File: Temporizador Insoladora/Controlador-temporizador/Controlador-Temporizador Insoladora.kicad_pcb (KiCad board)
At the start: 2 copper layers, 99.1 x 66 mm, 77 parts, among them P1 ICSP, P2 VAC12V, P3 CARGA, P4 TRANSF, P5 VAC, P6 OPTO, P7 CONN_02X08, P8 OPTO, P9 OPTO, Q1 BC548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

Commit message: Casi terminado controlador
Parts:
- moved C5 8.95 mm to (113.0, 116.2), turned to 180 degrees
- moved C13 3.81 mm to (193.7, 102.2)
- moved F1 3.81 mm to (174.6, 90.8)
- moved P3 3.81 mm to (210.2, 75.6)
- moved P4 3.81 mm to (200.0, 75.6)
- moved P5 3.81 mm to (187.3, 75.6)
- moved P8 3.81 mm to (184.8, 121.9)
- moved R15 3.81 mm to (188.6, 116.2)
- moved R18 3.81 mm to (182.2, 94.6)
- moved R19 3.81 mm to (187.3, 90.8)
- moved R23 3.81 mm to (191.1, 94.6)
- moved U3 3.81 mm to (184.8, 107.3)
- moved U4 3.81 mm to (194.9, 94.6)
- moved VR1 3.81 mm to (194.9, 81.9)
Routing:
- net VCC: track 134.1 -> 78.2 mm, vias 2 -> 3
- net Net-(D2-Pad1): track 22.6 -> 18.8 mm
- net Net-(D6-Pad1): track 6.66 -> 10.3 mm, vias 0 -> 1
- added copper zone on B.Cu, net VCC
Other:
- board size 99.1 x 66 mm -> 101.6 x 68.6 mm

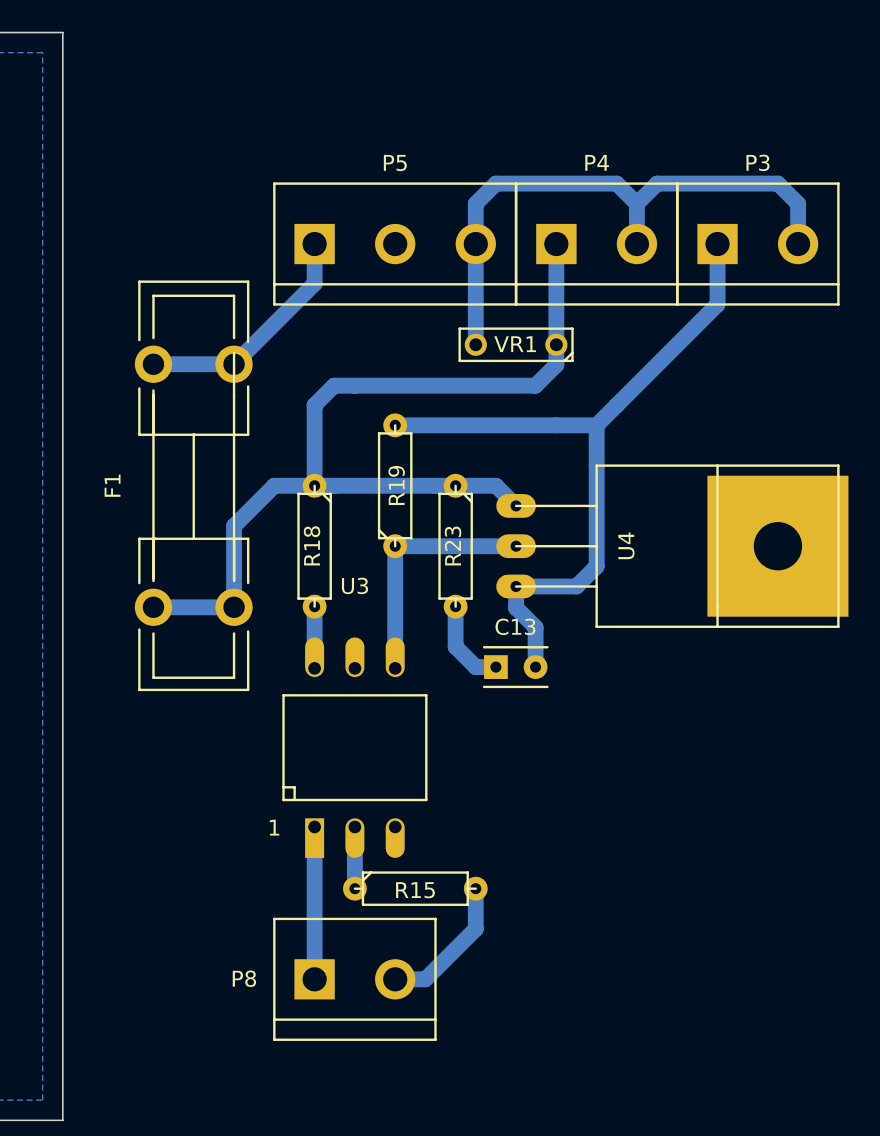
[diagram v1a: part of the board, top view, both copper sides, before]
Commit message: Acomodando la parte de potencia del controlador
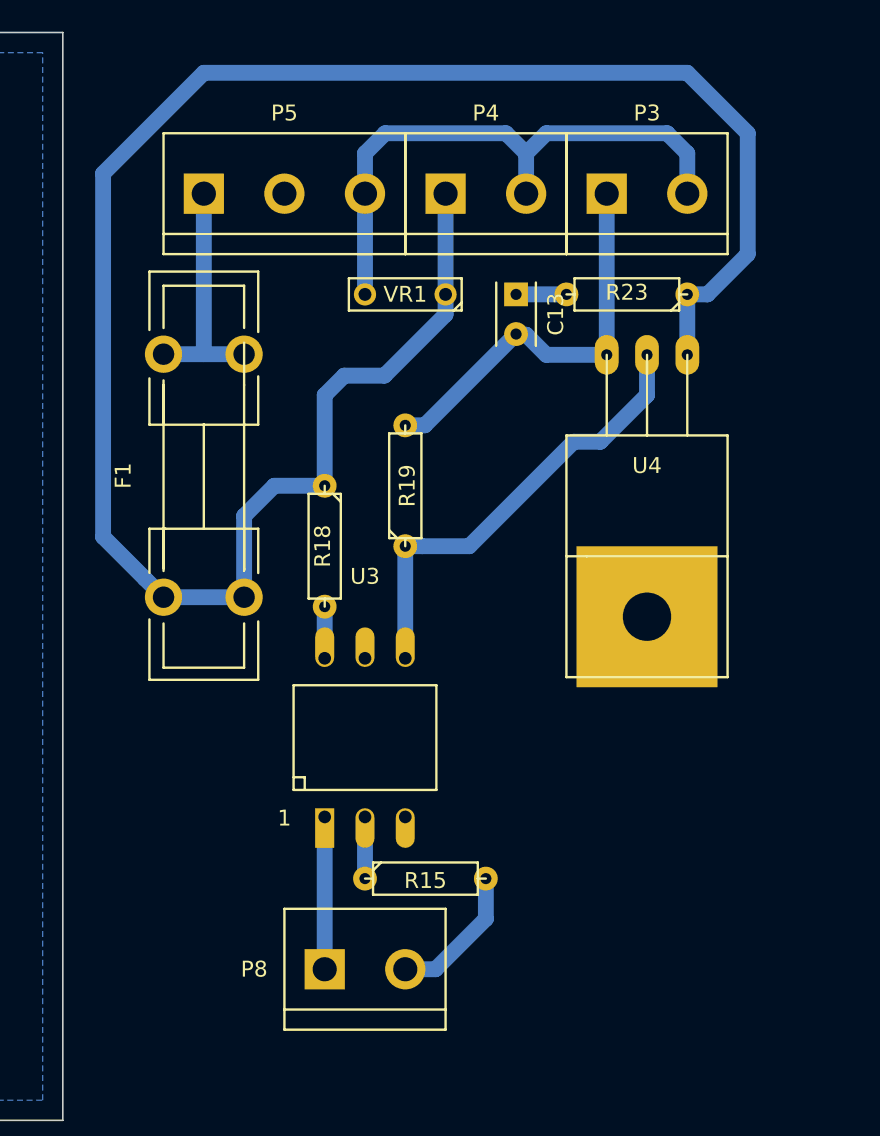
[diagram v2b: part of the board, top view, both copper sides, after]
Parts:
- moved C13 23.5 mm to (194.9, 78.7), turned to 270 degrees
- moved R23 19.2 mm to (201.9, 78.7), turned to 180 degrees
- moved U4 14.6 mm to (203.2, 82.5), turned to 270 degrees
- moved P3 7.67 mm to (203.2, 72.4)
- moved P4 7.67 mm to (193.0, 72.4)
- moved VR1 7.67 mm to (188.0, 78.7)
- moved P5 7.67 mm to (180.3, 72.4)
- moved F1 0.90 mm to (175.3, 90.2)
- moved P8 0.90 mm to (185.4, 121.3)
- moved R15 0.90 mm to (189.2, 115.6)
- moved U3 0.90 mm to (185.4, 106.7)
- moved R19 0.64 mm to (188.0, 90.8)
- moved R18 0.63 mm to (182.9, 94.6)
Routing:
- net Net-(F1-Pad1): track 58.6 -> 128.0 mm
- net Net-(C13-Pad2): track 47.4 -> 25.8 mm
- net Net-(R19-Pad1): track 15.3 -> 28.8 mm
- net Net-(C13-Pad1): track 5.61 -> 3.18 mm
- net Net-(R18-Pad2): track 3.89 -> 3.26 mm

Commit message: Casi termonado controlador, ver si los componentes se ajustan
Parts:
- C13: value 39nF -> 10nF; footprint Capacitors_ThroughHole:C_Rect_L4_W2.5_P2.5 -> Capacitors_ThroughHole:C_Rect_L7_W2.5_P5
- F1: value 1A -> 3A
- R19: moved to B.Cu
- R23: value 10 -> 39
- moved F1 31.8 mm to (207.0, 88.9)
- moved P3 22.9 mm to (180.3, 71.1)
- moved P5 22.9 mm to (203.2, 71.1)
- moved R23 12.8 mm to (189.2, 77.5)
- moved C13 12.1 mm to (182.9, 77.5), turned to 180 degrees
- moved R18 10.3 mm to (193.0, 96.5), turned to 180 degrees
- moved VR1 10.2 mm to (198.1, 77.5), turned to 0 degrees
- moved U4 8.98 mm to (196.8, 88.9), turned to 180 degrees
- moved R19 7.65 mm to (193.0, 85.1)
- moved U3 5.24 mm to (190.5, 105.4)
- moved P8 5.24 mm to (190.5, 120.0)
- moved R15 5.24 mm to (194.3, 114.3)
- moved P4 2.84 mm to (190.5, 71.1)
- moved R12 1.27 mm to (120.7, 97.8)
- moved R13 1.27 mm to (125.7, 102.9)
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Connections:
- P5 pad 1: Net-(F1-Pad2) -> Net-(P3-Pad2)
- P5 pad 3: Net-(P3-Pad2) -> Net-(F1-Pad2)
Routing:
- net Net-(F1-Pad1): track 128.0 -> 49.3 mm
- net Net-(R19-Pad1): track 28.8 -> 15.3 mm
- net Net-(P3-Pad2): track 36.4 -> 28.8 mm
- net Net-(C13-Pad2): track 25.8 -> 30.6 mm
- net SALIDAOPTO0: track 21.2 -> 18.4 mm
- net SALIDAOPTO1: track 16.8 -> 14.6 mm
- net Net-(R18-Pad2): track 3.26 -> 4.42 mm
- net VCC: track 78.2 -> 79.0 mm
- net Net-(C13-Pad1): track 3.18 -> 2.54 mm
- net Net-(Q1-Pad2): track 10.5 -> 11.0 mm
- added copper zone on B.Cu, net Net-(C13-Pad2)
- added copper zone on B.Cu, net Net-(F1-Pad1)
- added copper zone on B.Cu, net Net-(F1-Pad2)
- added copper zone on B.Cu, net Net-(P3-Pad2)
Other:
- board size 101.6 x 68.6 mm -> 147.3 x 68.6 mm

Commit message: Controlador finalizado
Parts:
- added P10: CONN_01X08, Socket_Strips:Socket_Strip_Straight_1x08, F.Cu at (104.1, 67.3)
- added REF**: MountingHole_2-5mm, Mounting_Holes:MountingHole_2-5mm, F.Cu at (160.0, 124.5)
- added REF**: MountingHole_2-5mm, Mounting_Holes:MountingHole_2-5mm, F.Cu at (71.1, 124.5)
- added REF**: MountingHole_2-5mm, Mounting_Holes:MountingHole_2-5mm, F.Cu at (71.1, 68.6)
- added REF**: MountingHole_2-5mm, Mounting_Holes:MountingHole_2-5mm, F.Cu at (160.0, 68.6)
- added REF**: MountingHole_2-5mm, Mounting_Holes:MountingHole_2-5mm, F.Cu at (171.4, 124.5)
- added REF**: MountingHole_2-5mm, Mounting_Holes:MountingHole_2-5mm, F.Cu at (201.9, 124.5)
- added REF**: MountingHole_2-5mm, Mounting_Holes:MountingHole_2-5mm, F.Cu at (201.9, 72.4)
- added REF**: MountingHole_2-5mm, Mounting_Holes:MountingHole_2-5mm, F.Cu at (171.4, 72.4)
- R14: value R -> 220
- moved R15 8.98 mm to (188.0, 120.7)
- moved R18 8.98 mm to (186.7, 102.9)
- moved U3 8.98 mm to (184.2, 111.8)
- moved C13 8.98 mm to (176.5, 83.8)
- moved F1 8.98 mm to (200.7, 95.3)
- moved P3 8.98 mm to (174.0, 77.5)
- moved P4 8.98 mm to (184.2, 77.5)
- moved P5 8.98 mm to (196.8, 77.5)
- moved P8 8.98 mm to (184.2, 126.4)
- moved R19 8.98 mm to (186.7, 91.4)
- moved R23 8.98 mm to (182.9, 83.8)
- moved U4 8.98 mm to (190.5, 95.2)
- moved VR1 8.98 mm to (191.8, 83.8)
- turned C4 to 270 degrees
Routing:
- net Net-(P10-Pad1): track 10.2 -> 25.2 mm
- net Net-(P10-Pad7): track 14.5 -> 27.4 mm
- net Net-(P10-Pad5): track 10.2 -> 19.6 mm
- net Net-(P10-Pad3): track 10.2 -> 19.4 mm
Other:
- board size 147.3 x 68.6 mm -> 141 x 68.6 mm

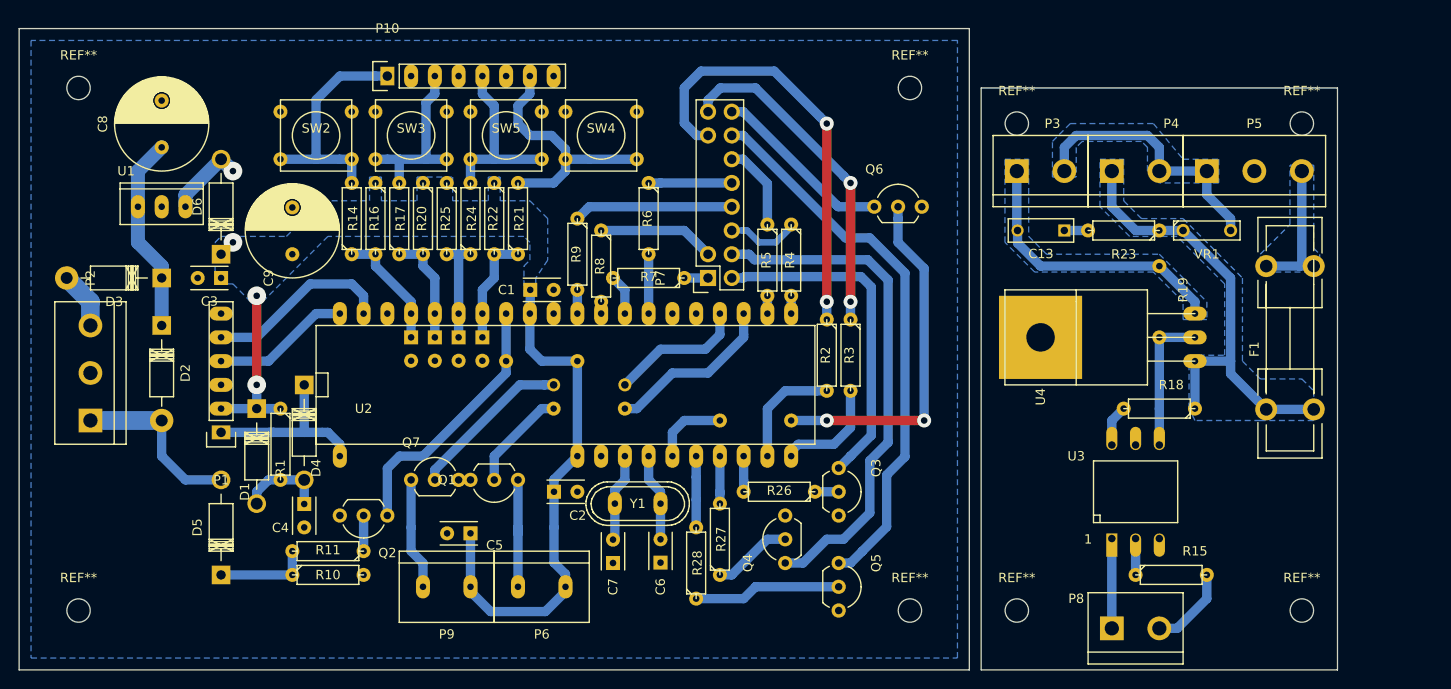
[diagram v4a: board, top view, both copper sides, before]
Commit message: Primer prueba de impresion de fotolitos
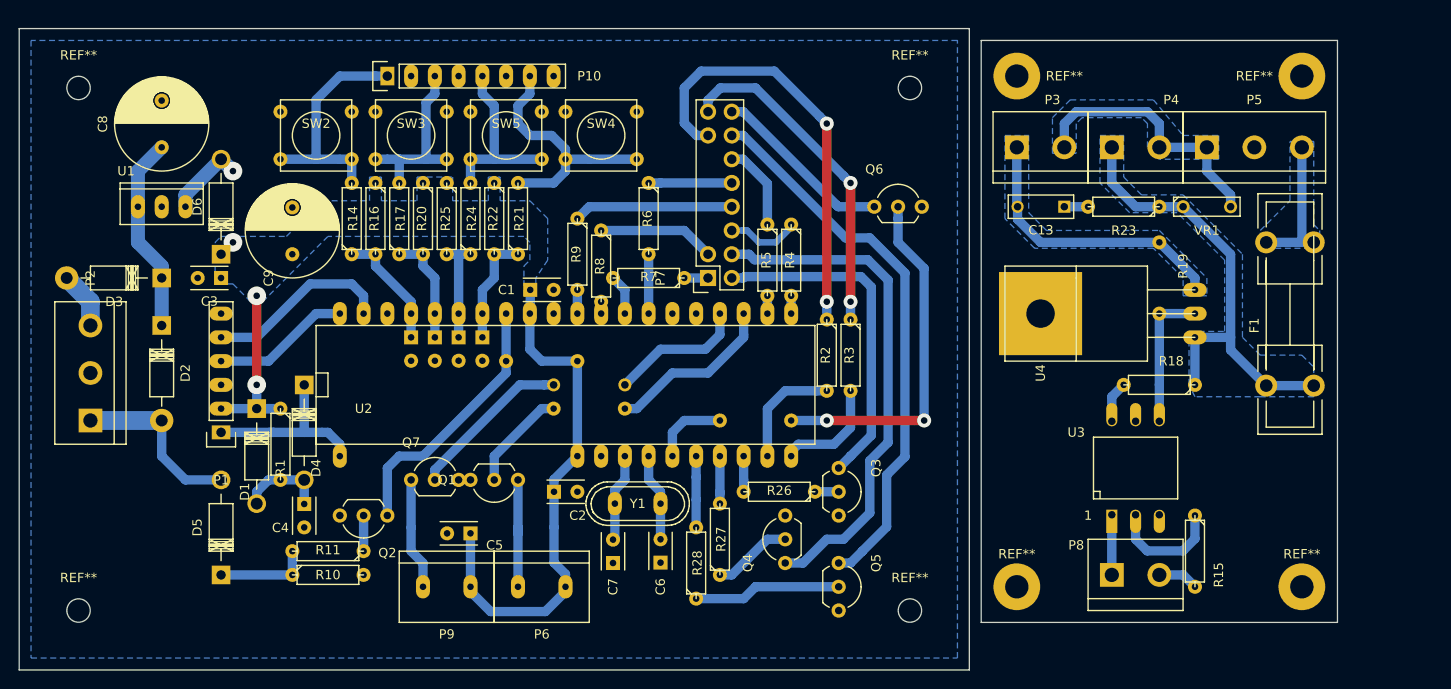
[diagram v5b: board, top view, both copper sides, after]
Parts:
- removed the REF** at (201.9, 124.5)
- removed the REF** at (201.9, 72.4)
- removed the REF** at (171.4, 72.4)
- added REF**: MountingHole_2-5mm, Mounting_Holes:MountingHole_2-5mm, F.Cu at (201.9, 67.3)
- added REF**: MountingHole_2-5mm, Mounting_Holes:MountingHole_2-5mm, F.Cu at (171.4, 67.3)
- added REF**: MountingHole_2-5mm, Mounting_Holes:MountingHole_2-5mm, F.Cu at (201.9, 121.9)
- moved P8 5.71 mm to (184.2, 120.7)
- moved R15 3.59 mm to (190.5, 118.1), turned to 270 degrees
- moved R18 2.54 mm to (186.7, 100.3)
- moved U3 2.54 mm to (184.2, 109.2)
- moved U4 2.54 mm to (190.5, 92.7)
- moved C13 2.54 mm to (176.5, 81.3)
- moved F1 2.54 mm to (200.7, 92.8)
- moved P3 2.54 mm to (174.0, 74.9)
- moved P4 2.54 mm to (184.2, 74.9)
- moved P5 2.54 mm to (196.8, 74.9)
- moved R19 2.54 mm to (186.7, 88.9)
- moved R23 2.54 mm to (182.9, 81.3)
- moved REF** 2.54 mm to (171.4, 121.9)
- moved VR1 2.54 mm to (191.8, 81.3)
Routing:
- net Net-(R15-Pad1): track 5.24 -> 15.4 mm
- net Net-(P8-Pad2): track 8.94 -> 4.34 mm
- net Net-(P8-Pad1): track 10.2 -> 7.06 mm
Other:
- outline, holes or cut-outs redrawn

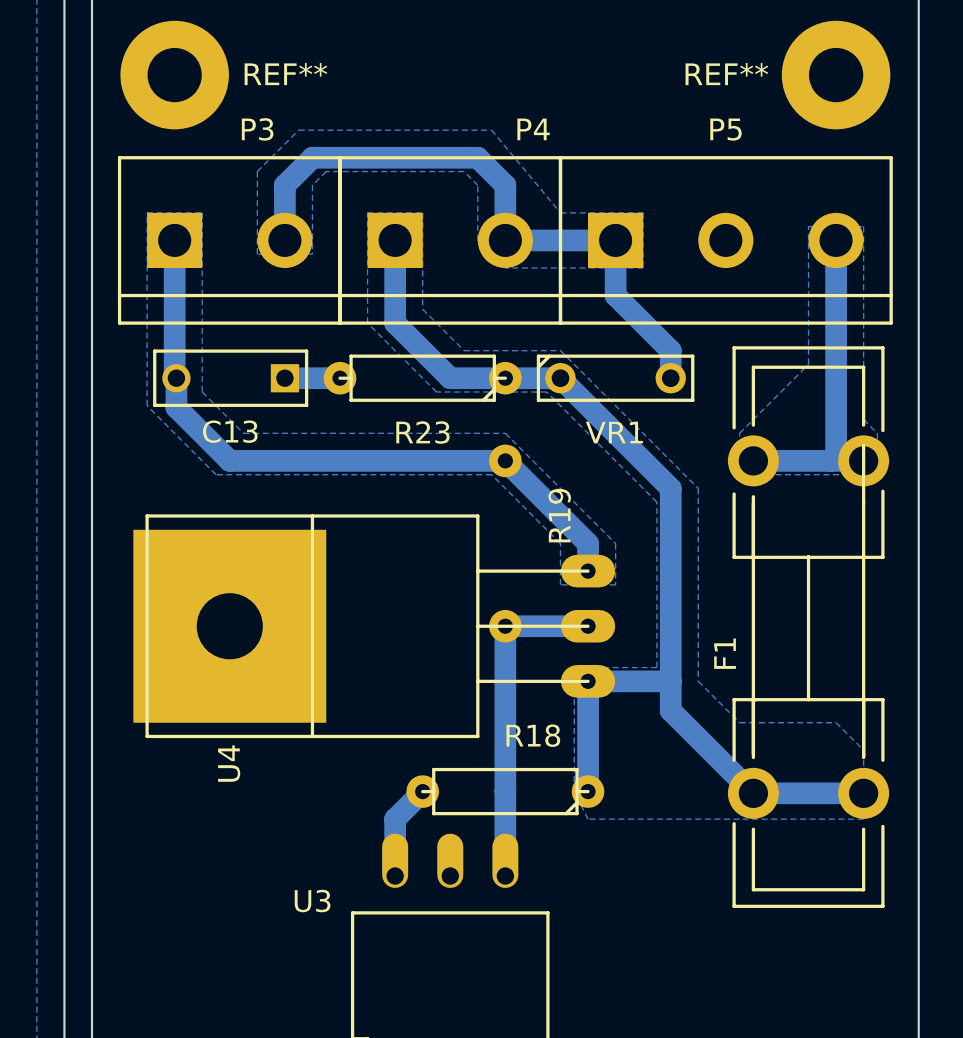
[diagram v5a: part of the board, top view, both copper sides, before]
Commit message: Cambiado tamaño de footprint del capacitor y varistor de la parte de potencia
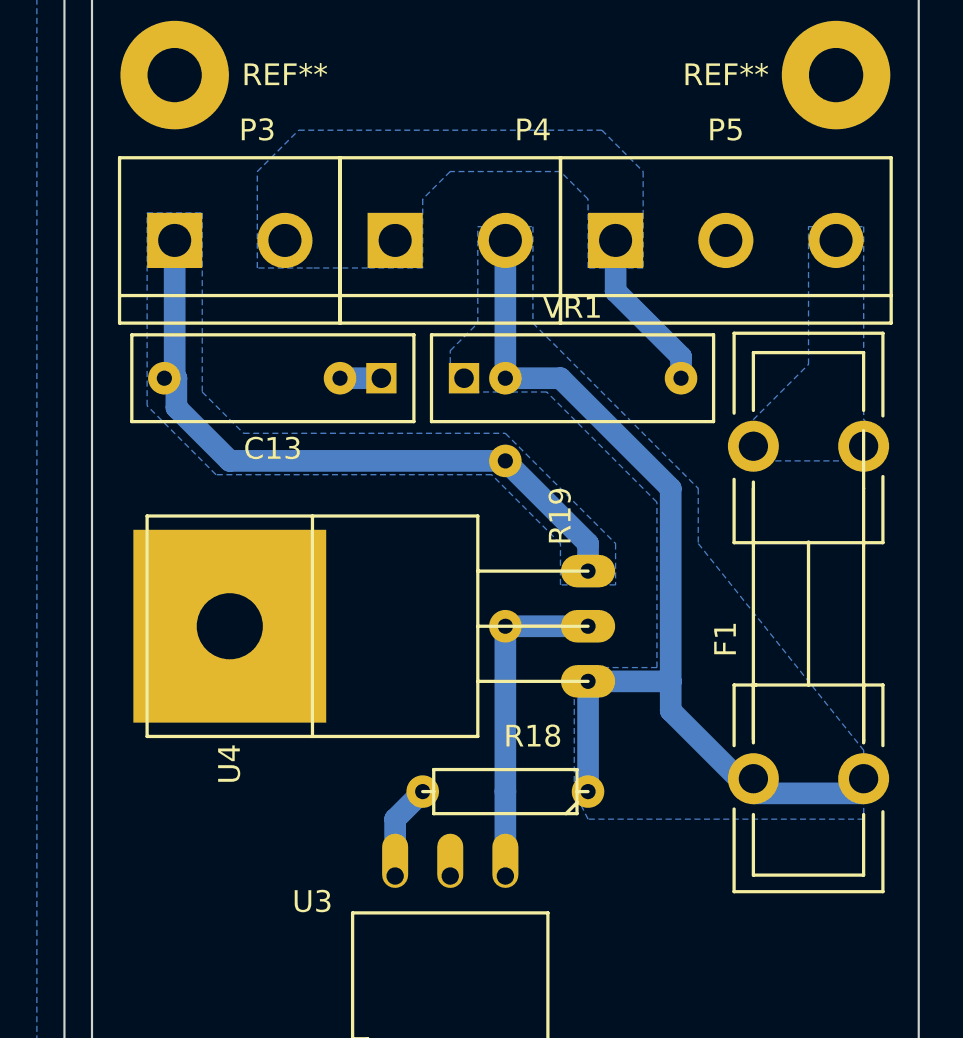
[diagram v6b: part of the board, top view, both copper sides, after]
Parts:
- C13: footprint Capacitors_ThroughHole:C_Rect_L7_W2.5_P5 -> Capacitors_ThroughHole:C_Rect_L13_W4_P10
- R23: moved to B.Cu
- VR1: footprint Discret:C2 -> Capacitors_ThroughHole:C_Rect_L13_W4_P10
- moved VR1 6.99 mm to (184.8, 81.3)
- moved C13 4.44 mm to (181.0, 81.3)
- moved F1 0.68 mm to (200.7, 92.1)
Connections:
- P4 pad 1: Net-(F1-Pad1) -> Net-(P3-Pad2)
- P4 pad 2: Net-(P3-Pad2) -> Net-(F1-Pad1)
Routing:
- net Net-(P3-Pad2): track 28.8 -> 7.60 mm
- net Net-(F1-Pad2): track 15.3 -> 0.00 mm
- net Net-(F1-Pad1): track 49.3 -> 45.7 mm
- net Net-(C13-Pad1): track 2.54 -> 1.91 mm
